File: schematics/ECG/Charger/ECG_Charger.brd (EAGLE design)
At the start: 27.3 x 27.3 mm, 7 parts, among them IC1 MCP73832_SOT23-5

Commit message: routed charger board
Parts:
- added C2: 4.7uF, rcl:C0805
- added CONN1: M80-4V, harwin:M80-4-V
- added CONN2: M80-6V, harwin:M80-6-V
- C1: device rcl:C0402 -> rcl:C0805
- R1, R2: device rcl:R0201 -> rcl:R0805
- moved USBCONN 22.8 mm to (13.4, 25.1), turned to 270 degrees
- moved LED1 20.5 mm to (5.82, 26.3), turned to 0 degrees
- moved FUSE 16.0 mm to (11.0, 19.6), turned to 0 degrees
- moved R1 14.3 mm to (5.74, 23.5), turned to 0 degrees
- moved C1 9.92 mm to (10.9, 17.2), turned to 180 degrees
- moved R2 9.60 mm to (14.9, 13.2), turned to 90 degrees
- moved IC1 6.28 mm to (10.9, 13.3), turned to 0 degrees
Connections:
- removed net VSS: R2.1
- net BATT: now also C2.1, CONN1.3
- net GND: now also C2.2, CONN1.4, R2.1
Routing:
- net STAT: track 0.00 -> 15.5 mm
- net VUSB: track 0.00 -> 13.4 mm
- net GND: track 0.00 -> 10.4 mm, vias 0 -> 4
- net BATT: track 0.00 -> 10.2 mm
- net VPROG: track 0.00 -> 3.20 mm
- net VUSB_5V: track 0.00 -> 2.85 mm
- net N$3: track 0.00 -> 2.80 mm
- added copper zone on layer 1, net GND

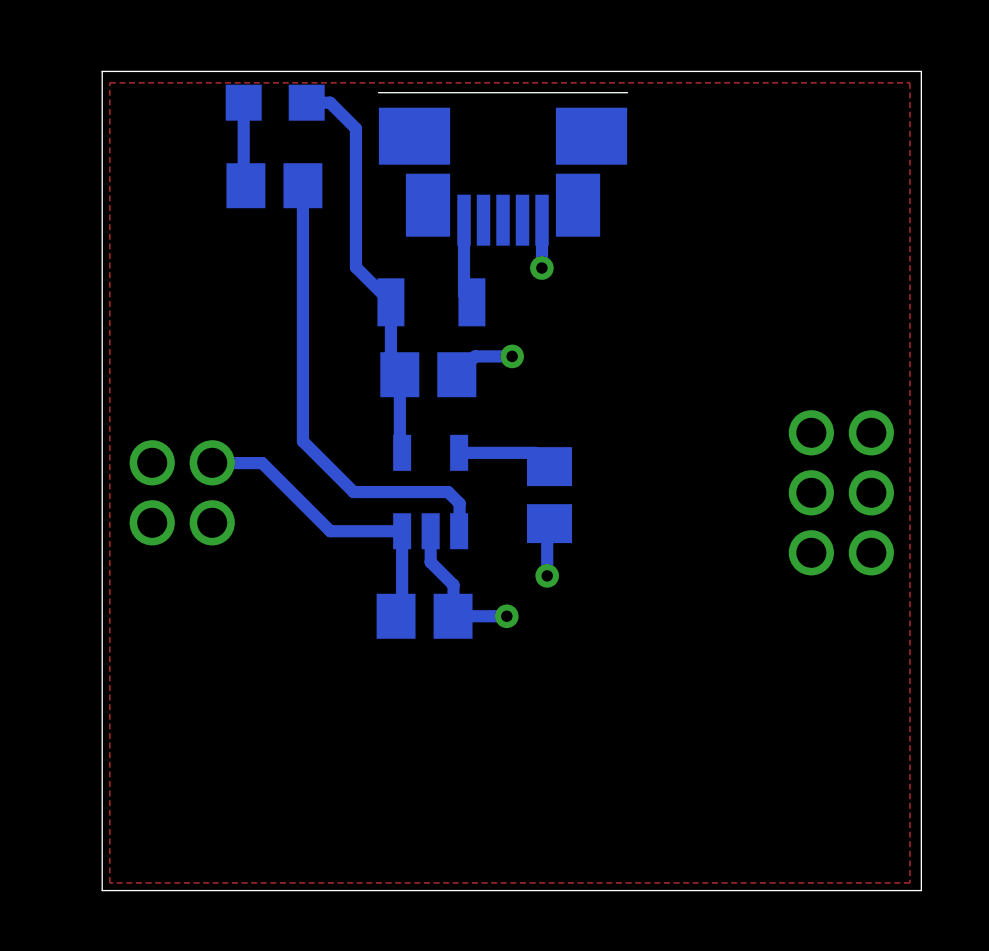
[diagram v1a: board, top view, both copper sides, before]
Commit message: switched ECG boards to spring loaded pin headers
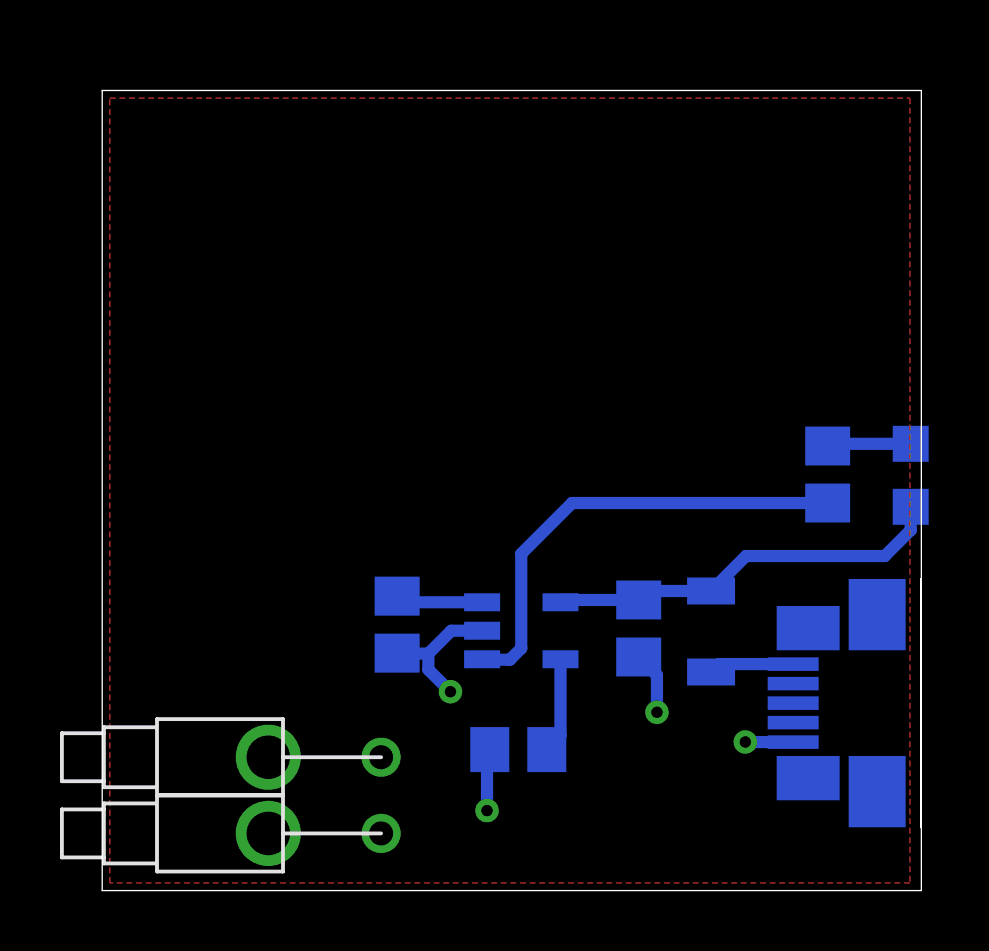
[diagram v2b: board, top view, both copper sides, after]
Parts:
- removed CONN1: M80-4V, harwin:M80-4-V
- removed CONN2: M80-6V, harwin:M80-6-V
- added U$1, U$2: PISTON_RA_TH, pins:PISTON_RA_TH
- moved LED1 24.5 mm to (26.9, 13.8), turned to 90 degrees
- moved USBCONN 22.6 mm to (25.8, 6.25), turned to 0 degrees
- moved R1 20.8 mm to (24.2, 13.9), turned to 90 degrees
- moved FUSE 14.4 mm to (20.3, 8.64), turned to 90 degrees
- moved C1 11.0 mm to (17.9, 8.74), turned to 270 degrees
- moved R2 8.55 mm to (13.9, 4.70), turned to 180 degrees
- moved IC1 5.52 mm to (14.0, 8.66), turned to 90 degrees
- moved C2 0.96 mm to (9.83, 8.86), turned to 270 degrees
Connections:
- net BATT: now also U$1.1; no longer CONN1.3
- net GND: now also U$2.1; no longer CONN1.4
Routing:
- net BATT: track 10.2 -> 2.92 mm
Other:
- board size 27.3 x 27.3 mm -> 27.3 x 26.7 mm

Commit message: redesigned patch board and charging board
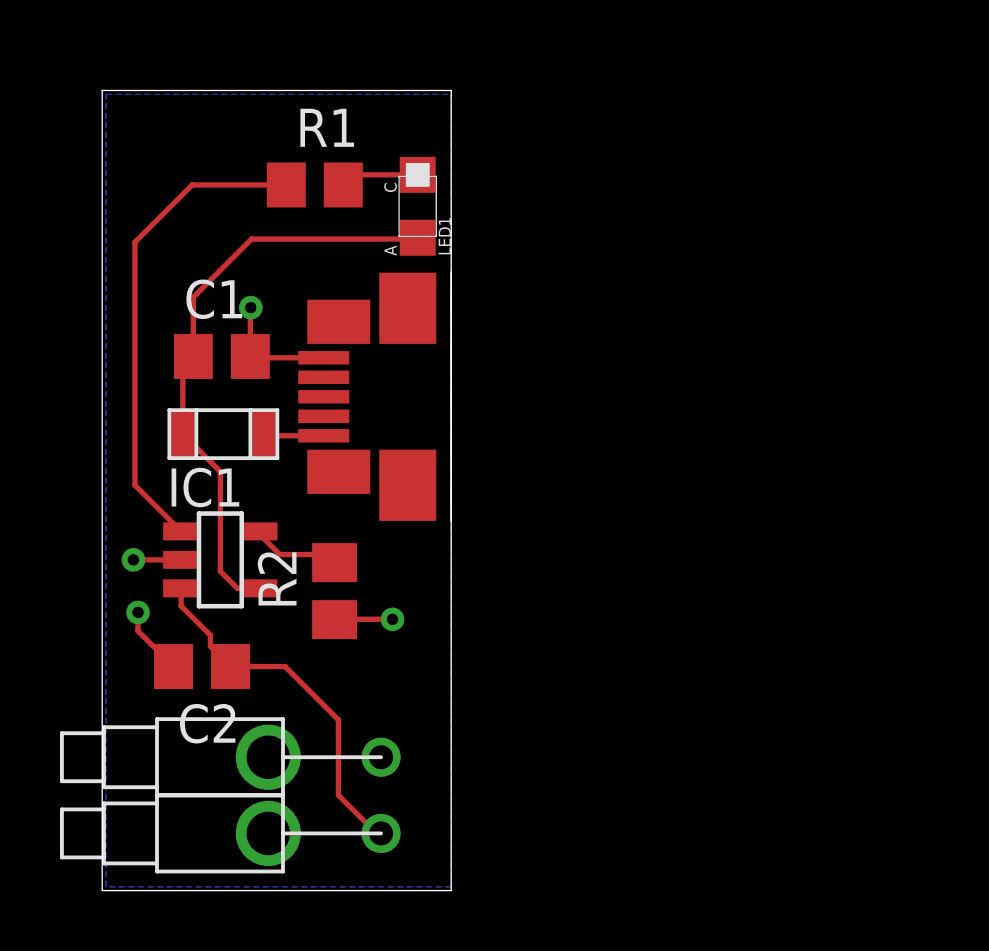
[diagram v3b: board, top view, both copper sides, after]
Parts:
- moved R1 19.6 mm to (7.09, 23.5), flipped to the top, turned to 0 degrees
- moved LED1 18.7 mm to (10.5, 22.8), flipped to the top
- moved USBCONN 18.7 mm to (10.2, 16.5), flipped to the top, turned to 180 degrees
- moved FUSE 17.5 mm to (4.04, 15.2), flipped to the top, turned to 180 degrees
- moved C1 16.6 mm to (3.99, 17.8), flipped to the top, turned to 0 degrees
- moved IC1 10.3 mm to (3.94, 11.0), flipped to the top, turned to 270 degrees
- moved R2 8.09 mm to (7.75, 9.98), flipped to the top, turned to 90 degrees
- moved C2 6.65 mm to (3.33, 7.47), flipped to the top, turned to 180 degrees
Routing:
- net BATT: track 2.92 -> 12.1 mm
- net VUSB: track 13.4 -> 19.8 mm
- net VUSB_5V: track 2.85 -> 2.05 mm
- net GND: track 10.7 -> 9.95 mm
- net STAT: track 15.5 -> 16.1 mm
- added copper zone on layer 16, net GND
- removed copper zone on layer 1, net GND
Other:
- board size 27.3 x 26.7 mm -> 11.6 x 26.7 mm

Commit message: updated all boards to slightly larger dimensions and new target/piston positions
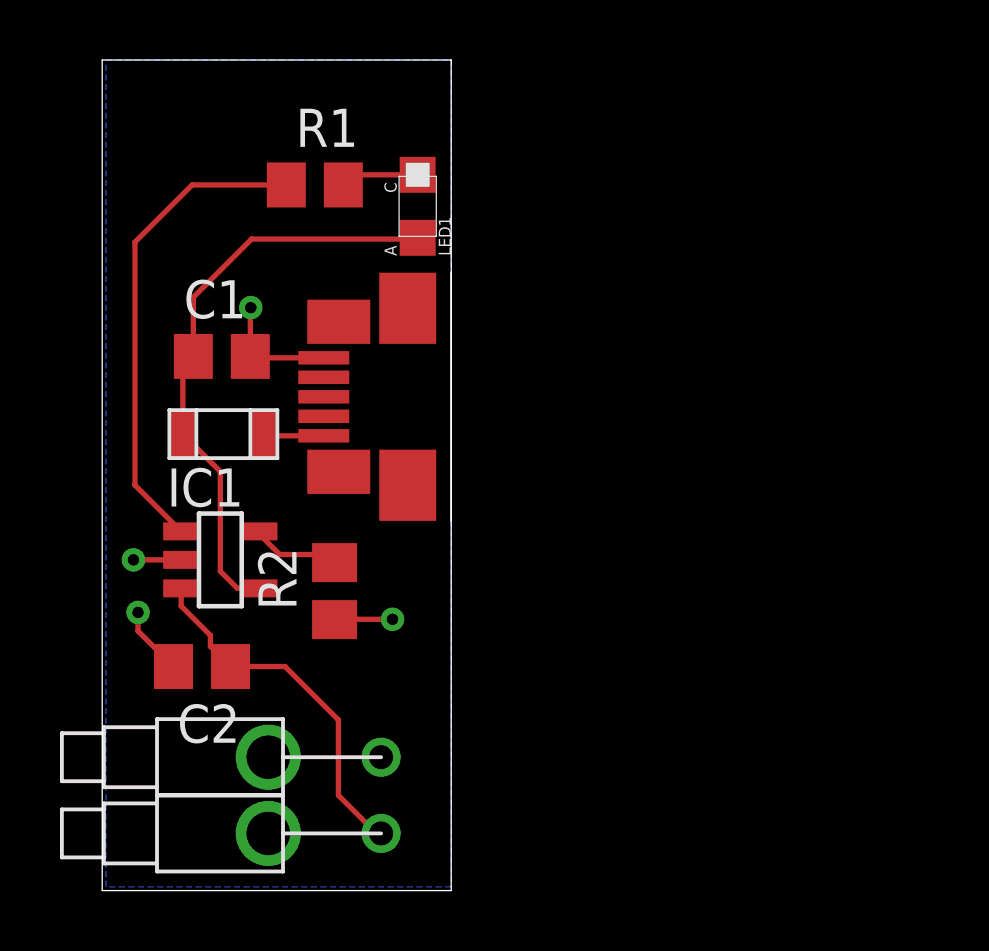
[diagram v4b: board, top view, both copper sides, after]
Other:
- board size 11.6 x 26.7 mm -> 11.6 x 27.7 mm
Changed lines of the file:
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@@
 <plain>
 <wire x1="0" y1="0" x2="11.6332" y2="0" width="0" layer="20"/>
-<wire x1="11.6332" y1="0" x2="11.6332" y2="26.67" width="0" layer="20"/>
-<wire x1="11.6332" y1="26.67" x2="0" y2="26.67" width="0" layer="20"/>
-<wire x1="0" y1="26.67" x2="0" y2="0" width="0" layer="20"/>
+<wire x1="11.6332" y1="0" x2="11.6332" y2="27.686" width="0" layer="20"/>
+<wire x1="11.6332" y1="27.686" x2="0" y2="27.686" width="0" layer="20"/>
+<wire x1="0" y1="27.686" x2="0" y2="0" width="0" layer="20"/>
 </plain>
 <attributes>
@@
 <contactref element="U$2" pad="1"/>
 <polygon width="0.1778" layer="16">
-<vertex x="0.127" y="26.543"/>
-<vertex x="11.6332" y="26.543"/>
+<vertex x="0.127" y="27.686"/>
+<vertex x="11.6332" y="27.686"/>
 <vertex x="11.6332" y="0.127"/>
 <vertex x="0.127" y="0.127"/>
